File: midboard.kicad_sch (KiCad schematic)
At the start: 7 parts, among them J14 Conn_02x13_Odd_Even

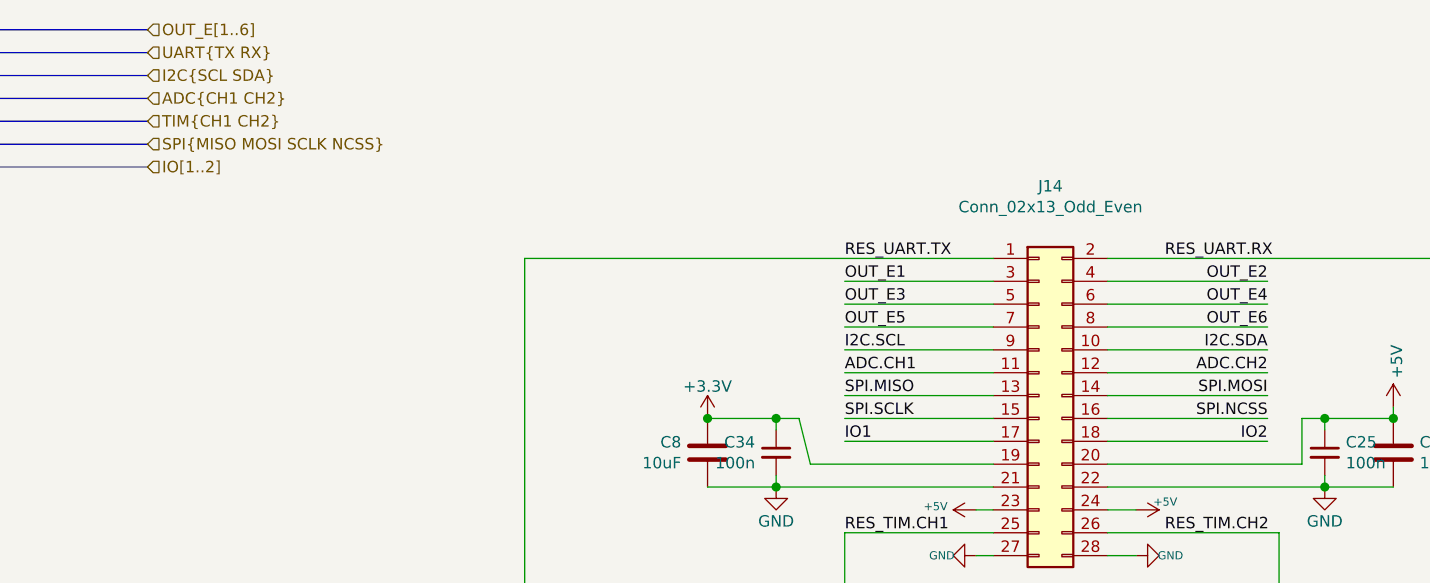
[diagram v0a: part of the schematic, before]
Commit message: UPDATE - LAN chipset waiting for verification
Signed-off-by: Jacek <matuszewski.kartech@gmail.com>
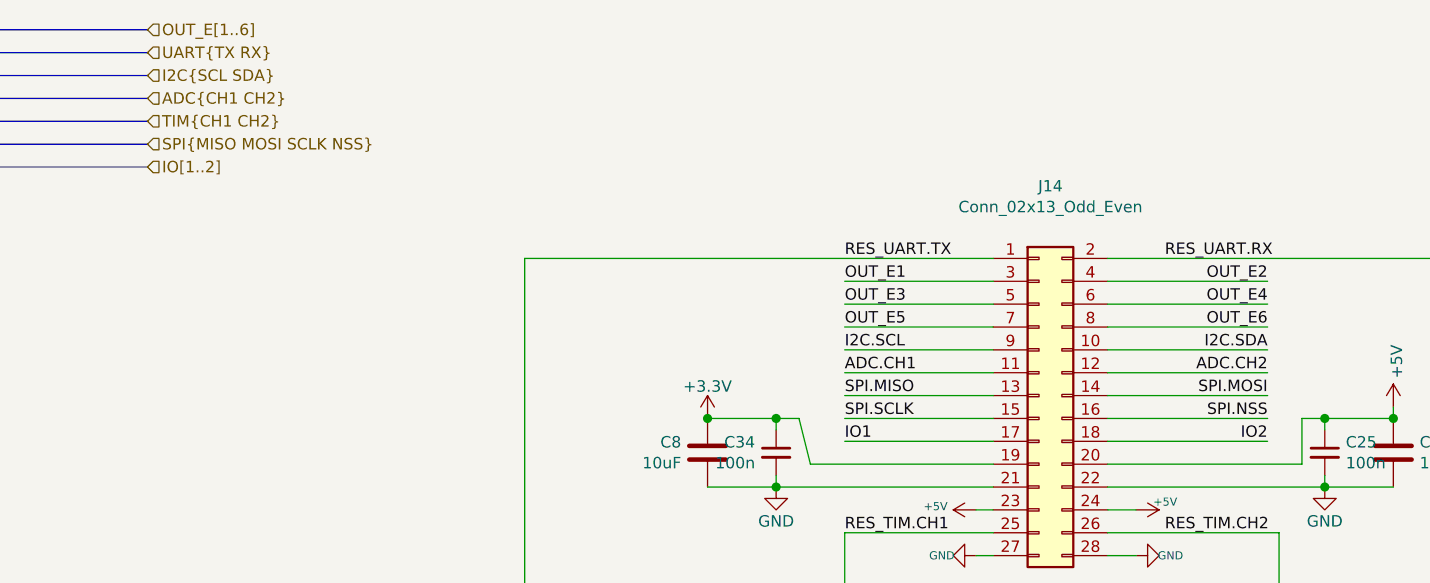
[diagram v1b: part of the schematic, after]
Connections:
- net SPI.NCSS renamed SPI.NSS
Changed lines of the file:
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@@
 (kicad_sch (version 20201015) (generator eeschema)
-  (page 1 12)
   (paper "A4")
   (junction (at 59.69 105.41) (diameter 1.016) (color 0 0 0 0))
@@
     (effects (font (size 1.27 1.27)) (justify right bottom))
   )
-  (label "SPI.NCSS" (at 213.36 78.74 180)
+  (label "SPI.NSS" (at 213.36 78.74 180)
     (effects (font (size 1.27 1.27)) (justify right bottom))
   )
@@
     (effects (font (size 1.27 1.27)) (justify left))
   )
-  (hierarchical_label "SPI{MISO MOSI SCLK NCSS}" (shape input) (at 88.9 48.26 0)
-    (effects (font (size 1.27 1.27)) (justify left))
-  )
+  (hierarchical_label "SPI{MISO MOSI SCLK NSS}" (shape input) (at 88.9 48.26 0)
+    (effects (font (size 1.27 1.27)) (justify left))
+  )

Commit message: Fixes
Signed-off-by: Jarosław Karwik <jaroslaw.karwik@gmail.com>
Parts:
- C25, C34: TME C0603C104K3RAC -> (none)
- C38, C8: footprint Capacitor_SMD:C_1206_3216Metric -> Capacitor_SMD:C_0603_1608Metric; TME 0805X106K100CT -> (none)
- RN9: TME (none) -> DR1206-100R-4/8
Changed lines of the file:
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@@
       (effects (font (size 1.27 1.27)) hide)
     )
-    (property "TME" "C0603C104K3RAC" (id 4) (at 158.75 82.55 0)
+    (property "TME" "" (id 4) (at 158.75 82.55 0)
       (effects (font (size 1.27 1.27)) hide)
     )
@@
       (effects (font (size 1.27 1.27)) hide)
     )
-    (property "TME" "C0603C104K3RAC" (id 4) (at 219.71 82.55 0)
+    (property "TME" "" (id 4) (at 219.71 82.55 0)
       (effects (font (size 1.27 1.27)) hide)
     )
@@
       (effects (font (size 1.27 1.27)) (justify left))
     )
-    (property "Footprint" "Capacitor_SMD:C_1206_3216Metric" (id 2) (at 150.1648 86.36 0)
+    (property "Footprint" "Capacitor_SMD:C_0603_1608Metric" (id 2) (at 150.1648 86.36 0)
       (effects (font (size 1.27 1.27)) hide)
     )
@@
       (effects (font (size 1.27 1.27)) hide)
     )
-    (property "TME" "0805X106K100CT" (id 4) (at 151.13 82.55 0)
+    (property "TME" "" (id 4) (at 151.13 82.55 0)
       (effects (font (size 1.27 1.27)) hide)
     )
@@
       (effects (font (size 1.27 1.27)) (justify left))
     )
-    (property "Footprint" "Capacitor_SMD:C_1206_3216Metric" (id 2) (at 228.2952 86.36 0)
+    (property "Footprint" "Capacitor_SMD:C_0603_1608Metric" (id 2) (at 228.2952 86.36 0)
       (effects (font (size 1.27 1.27)) hide)
     )
@@
       (effects (font (size 1.27 1.27)) hide)
     )
-    (property "TME" "0805X106K100CT" (id 4) (at 227.33 82.55 0)
+    (property "TME" "" (id 4) (at 227.33 82.55 0)
       (effects (font (size 1.27 1.27)) hide)
     )
@@
       (effects (font (size 1.27 1.27)) hide)
     )
+    (property "TME" "DR1206-100R-4/8" (id 4) (at 113.03 110.49 0)
+      (effects (font (size 1.27 1.27)) hide)
+    )

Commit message: UPDATE - 3D and Jumper descriptions
Signed-off-by: Jacek <matuszewski.kartech@gmail.com>
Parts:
- C25, C34: TME (none) -> C0603C104K3RAC
- C38, C8: TME (none) -> CL10A106MQ8NNNC
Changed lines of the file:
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@@
-(kicad_sch (version 20201015) (generator eeschema)
+(kicad_sch (version 20210126) (generator eeschema)
   (paper "A4")
   (junction (at 59.69 105.41) (diameter 1.016) (color 0 0 0 0))
@@
       (effects (font (size 1.27 1.27)) hide)
     )
+    (pin "1")
   )
   (symbol (lib_id "power:+3V3") (at 80.01 121.92 0) (mirror y) (unit 1)
@@
       (effects (font (size 1.27 1.27)) hide)
     )
+    (pin "1")
   )
   (symbol (lib_id "power:+3V3") (at 151.13 78.74 0) (mirror y) (unit 1)
@@
       (effects (font (size 1.27 1.27)) hide)
     )
+    (pin "1")
   )
   (symbol (lib_id "mfc_base_lib:+5V") (at 180.975 88.9 90) (unit 1)
@@
       (effects (font (size 1.27 1.27)) hide)
     )
+    (pin "1")
   )
   (symbol (lib_id "mfc_base_lib:+5V") (at 198.755 88.9 270) (unit 1)
@@
       (effects (font (size 1.27 1.27)) hide)
     )
+    (pin "1")
   )
   (symbol (lib_id "mfc_base_lib:+5V") (at 227.33 77.47 0) (unit 1)
@@
       (effects (font (size 1.27 1.27)) hide)
     )
+    (pin "1")
   )
   (symbol (lib_id "Uni_Printer-rescue:GND-Sensor_tank_v1-rescue-Uni_General_v1-rescue-Uni_Printer_v1-rescue") (at 71.12 137.16 0) (mirror y) (unit 1)
@@
       (effects (font (size 1.27 1.27)) hide)
     )
+    (pin "1")
   )
   (symbol (lib_id "Uni_Printer-rescue:GND-Sensor_tank_v1-rescue-Uni_General_v1-rescue-Uni_Printer_v1-rescue") (at 80.01 137.16 0) (mirror y) (unit 1)
@@
       (effects (font (size 1.27 1.27)) hide)
     )
+    (pin "1")
   )
   (symbol (lib_id "Uni_Printer-rescue:GND-Sensor_tank_v1-rescue-Uni_General_v1-rescue-Uni_Printer_v1-rescue") (at 158.75 86.36 0) (mirror y) (unit 1)
@@
       (effects (font (size 1.27 1.27)) hide)
     )
+    (pin "1")
   )
   (symbol (lib_id "Uni_Printer-rescue:GND-Sensor_tank_v1-rescue-Uni_General_v1-rescue-Uni_Printer_v1-rescue") (at 180.975 93.98 270) (mirror x) (unit 1)
@@
       (effects (font (size 1.27 1.27)) hide)
     )
+    (pin "1")
   )
   (symbol (lib_id "Uni_Printer-rescue:GND-Sensor_tank_v1-rescue-Uni_General_v1-rescue-Uni_Printer_v1-rescue") (at 198.755 93.98 90) (mirror x) (unit 1)
@@
       (effects (font (size 1.27 1.27)) hide)
     )
+    (pin "1")
   )
   (symbol (lib_id "Uni_Printer-rescue:GND-Sensor_tank_v1-rescue-Uni_General_v1-rescue-Uni_Printer_v1-rescue") (at 219.71 86.36 0) (unit 1)
@@
       (effects (font (size 1.27 1.27)) hide)
     )
+    (pin "1")
   )
   (symbol (lib_id "Uni_Printer-rescue:C_Small-Device") (at 158.75 82.55 0) (mirror y) (unit 1)
@@
       (effects (font (size 1.27 1.27)) hide)
     )
-    (property "TME" "" (id 4) (at 158.75 82.55 0)
-      (effects (font (size 1.27 1.27)) hide)
-    )
+    (property "TME" "C0603C104K3RAC" (id 4) (at 158.75 82.55 0)
+      (effects (font (size 1.27 1.27)) hide)
+    )
+    (pin "1")
+    (pin "2")
   )
   (symbol (lib_id "Uni_Printer-rescue:C_Small-Device") (at 219.71 82.55 0) (unit 1)
@@
       (effects (font (size 1.27 1.27)) hide)
     )
-    (property "TME" "" (id 4) (at 219.71 82.55 0)
-      (effects (font (size 1.27 1.27)) hide)
-    )
+    (property "TME" "C0603C104K3RAC" (id 4) (at 219.71 82.55 0)
+      (effects (font (size 1.27 1.27)) hide)
+    )
+    (pin "1")
+    (pin "2")
   )
   (symbol (lib_id "Uni_Printer-rescue:C-Device") (at 151.13 82.55 0) (mirror y) (unit 1)
@@
       (effects (font (size 1.27 1.27)) hide)
     )
-    (property "TME" "" (id 4) (at 151.13 82.55 0)
-      (effects (font (size 1.27 1.27)) hide)
-    )
+    (property "TME" "CL10A106MQ8NNNC" (id 4) (at 151.13 82.55 0)
+      (effects (font (size 1.27 1.27)) hide)
+    )
+    (pin "1")
+    (pin "2")
   )
   (symbol (lib_id "Uni_Printer-rescue:C-Device") (at 227.33 82.55 0) (unit 1)
@@
       (effects (font (size 1.27 1.27)) hide)
     )
-    (property "TME" "" (id 4) (at 227.33 82.55 0)
-      (effects (font (size 1.27 1.27)) hide)
-    )
+    (property "TME" "CL10A106MQ8NNNC" (id 4) (at 227.33 82.55 0)
+      (effects (font (size 1.27 1.27)) hide)
+    )
+    (pin "1")
+    (pin "2")
   )
   (symbol (lib_id "Uni_Printer-rescue:D_Schottky_x4_BAV99S-RESCUE-step2cnc-Sensor_tank_v1-rescue-Uni_General_v1-rescue-Uni_Printer_v1-rescue") (at 71.12 129.54 270) (mirror x) (unit 1)
@@
       (effects (font (size 1.27 1.27)) hide)
     )
+    (pin "1")
+    (pin "2")
+    (pin "6")
   )
   (symbol (lib_id "Uni_Printer-rescue:D_Schottky_x4_BAV99S-RESCUE-step2cnc-Sensor_tank_v1-rescue-Uni_General_v1-rescue-Uni_Printer_v1-rescue") (at 80.01 129.54 270) (mirror x) (unit 2)
@@
       (effects (font (size 1.27 1.27)) hide)
     )
+    (pin "3")
+    (pin "4")
+    (pin "5")
   )
   (symbol (lib_id "Uni_Printer-rescue:R_Pack04-Device") (at 113.03 110.49 270) (unit 1)
@@
       (effects (font (size 1.27 1.27)) hide)
     )
+    (pin "1")
+    (pin "2")
+    (pin "3")
+    (pin "4")
+    (pin "5")
+    (pin "6")
+    (pin "7")
+    (pin "8")
   )
   (symbol (lib_id "Connector_Generic:Conn_02x14_Odd_Even") (at 187.96 76.2 0) (unit 1)
@@
       (effects (font (size 1.27 1.27)) hide)
     )
+    (pin "1")
+    (pin "10")
+    (pin "11")
+    (pin "12")
+    (pin "13")
+    (pin "14")
+    (pin "15")
+    (pin "16")
+    (pin "17")
+    (pin "18")
+    (pin "19")
+    (pin "2")
+    (pin "20")
+    (pin "21")
+    (pin "22")
+    (pin "23")
+    (pin "24")
+    (pin "25")
+    (pin "26")
+    (pin "27")
+    (pin "28")
+    (pin "3")
+    (pin "4")
+    (pin "5")
+    (pin "6")
+    (pin "7")
+    (pin "8")
+    (pin "9")
   )
 )
